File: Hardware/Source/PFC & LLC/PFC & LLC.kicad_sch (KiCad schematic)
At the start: 0 parts

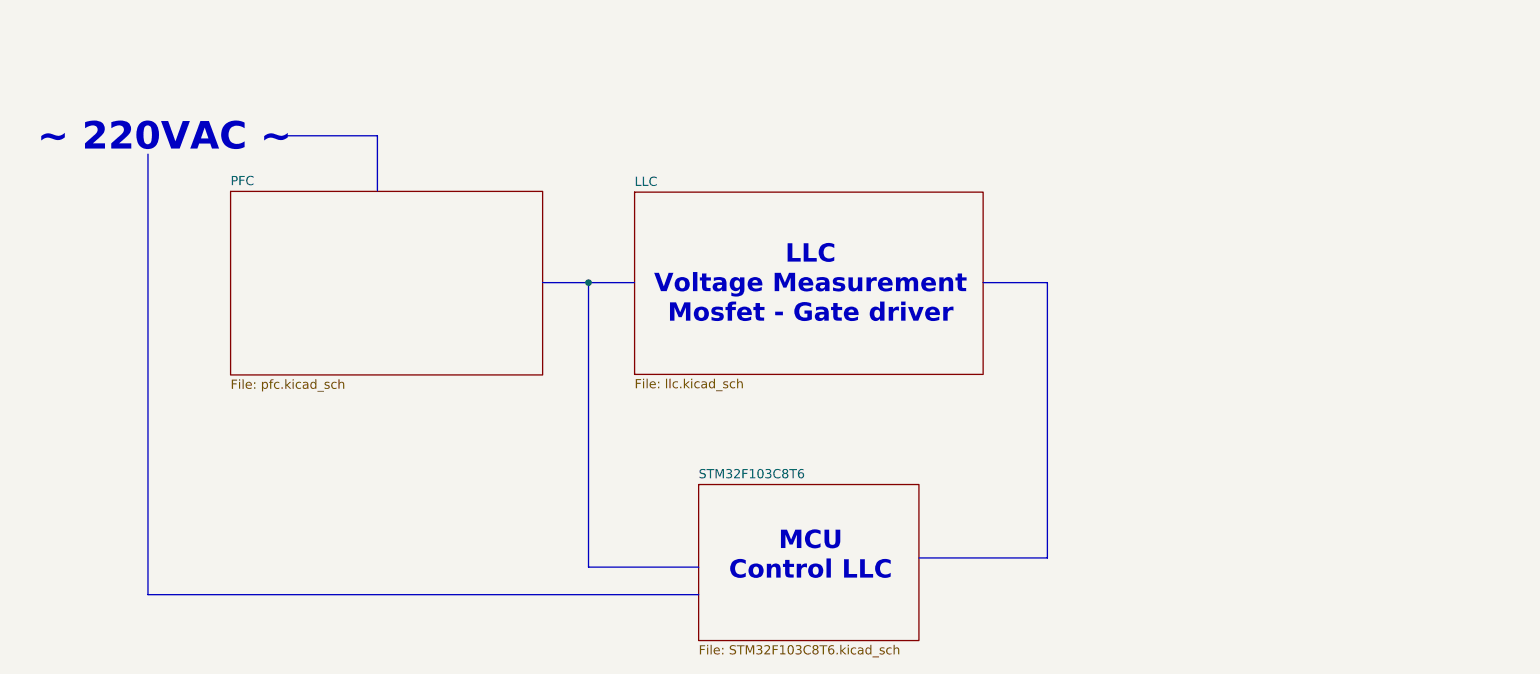
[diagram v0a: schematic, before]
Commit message: update ver 2.0 PFC-LLC
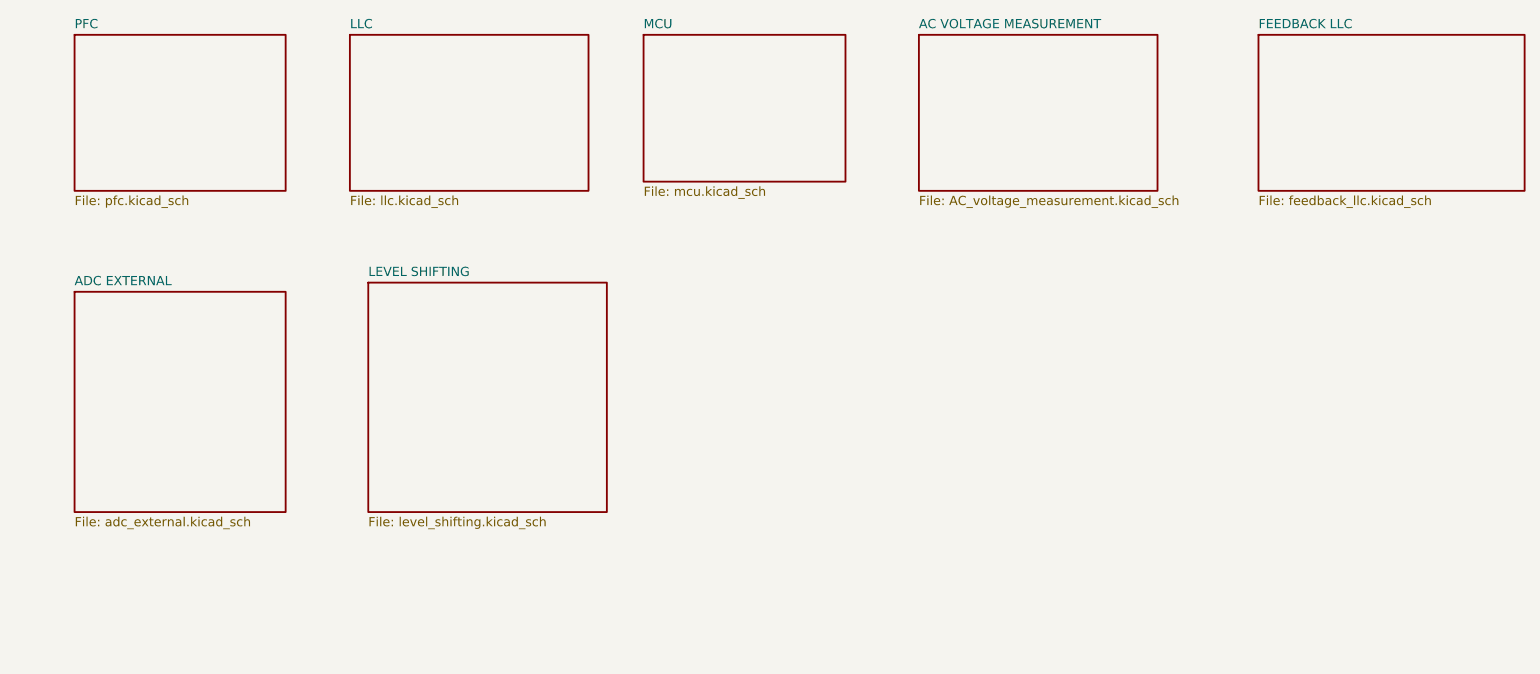
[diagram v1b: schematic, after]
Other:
- removed sheet STM32F103C8T6
- added sheet AC VOLTAGE MEASUREMENT (AC_voltage_measurement.kicad_sch)
- added sheet ADC EXTERNAL (adc_external.kicad_sch)
- added sheet FEEDBACK LLC (feedback_llc.kicad_sch)
- added sheet LEVEL SHIFTING (level_shifting.kicad_sch)
- added sheet MCU (mcu.kicad_sch)
- note removed: "LLC Voltage Measurement Mosfet - Gate driver"
- note removed: "MCU Control LLC"
- note removed: "~ 220VAC ~"
- company: (none) -> Ho Chi Minh City University of Technology - HCMUT
- title: (none) -> PFC & LLC

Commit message: update FEEDBACK, AC
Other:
- added sheet DETECT BATTERY (detect_battery.kicad_sch)
- added sheet POWER SUPPLY (power_supply.kicad_sch)
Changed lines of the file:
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@@
+	)
+	(sheet
+		(at 165.1 68.58)
+		(size 27.94 31.75)
+		(fields_autoplaced yes)
+		(stroke
+			(width 0.254)
+			(type solid)
+		)
+		(fill
+			(color 0 0 0 0.0000)
+		)
+		(property "Sheetname" "POWER SUPPLY"
+			(at 165.1 67.8176 0)
+			(effects
+				(font
+					(size 1.27 1.27)
+				)
+				(justify left bottom)
+			)
+		)
+		(property "Sheetfile" "power_supply.kicad_sch"
+			(at 165.1 100.9654 0)
+			(effects
+				(font
+					(size 1.27 1.27)
+				)
+				(justify left top)
+			)
+		)
+		(instances
+			(project "PFC & LLC"
+				(path "/97d1a1fe-d5a5-4da8-b78a-88a9132d14ad"
+					(page "10")
+				)
+			)
+		)
 	)
 	(sheet
@@
 				)
 			)
+		)
+	)
+	(sheet
+		(at 128.27 68.58)
+		(size 25.4 31.75)
+		(fields_autoplaced yes)
+		(stroke
+			(width 0.254)
+			(type solid)
+		)
+		(fill
+			(color 0 0 0 0.0000)
+		)
+		(property "Sheetname" "DETECT BATTERY"
+			(at 128.27 67.8176 0)
+			(effects
+				(font
+					(size 1.27 1.27)
+				)
+				(justify left bottom)
+			)
+		)
+		(property "Sheetfile" "detect_battery.kicad_sch"
+			(at 128.27 100.9654 0)
+			(effects
+				(font
+					(size 1.27 1.27)
+				)
+				(justify left top)
+			)
+		)
+		(instances
+			(project "PFC & LLC"
+				(path "/97d1a1fe-d5a5-4da8-b78a-88a9132d14ad"
+					(page "9")
+				)
+			)

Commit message: update lib, LLC
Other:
- added sheet ENABLE LLC PFC (enable_LLC_PFC.kicad_sch)
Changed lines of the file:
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@@
 	)
 	(sheet
-		(at 165.1 68.58)
-		(size 27.94 31.75)
+		(at 165.1 74.93)
+		(size 39.37 21.59)
 		(fields_autoplaced yes)
 		(stroke
@@
 		)
 		(property "Sheetname" "POWER SUPPLY"
-			(at 165.1 67.8176 0)
+			(at 165.1 74.1676 0)
 			(effects
 				(font
@@
 		)
 		(property "Sheetfile" "power_supply.kicad_sch"
-			(at 165.1 100.9654 0)
+			(at 165.1 97.1554 0)
 			(effects
 				(font
@@
 	)
 	(sheet
-		(at 212.09 34.29)
+		(at 210.82 34.29)
 		(size 36.83 21.59)
 		(fields_autoplaced yes)
@@
 		)
 		(property "Sheetname" "FEEDBACK LLC"
-			(at 212.09 33.5276 0)
+			(at 210.82 33.5276 0)
 			(effects
 				(font
@@
 		)
 		(property "Sheetfile" "feedback_llc.kicad_sch"
-			(at 212.09 56.5154 0)
+			(at 210.82 56.5154 0)
 			(effects
 				(font
@@
 	)
 	(sheet
-		(at 128.27 68.58)
-		(size 25.4 31.75)
+		(at 124.46 66.04)
+		(size 39.37 31.75)
 		(fields_autoplaced yes)
 		(stroke
@@
 		)
 		(property "Sheetname" "DETECT BATTERY"
-			(at 128.27 67.8176 0)
+			(at 124.46 65.2776 0)
 			(effects
 				(font
@@
 		)
 		(property "Sheetfile" "detect_battery.kicad_sch"
-			(at 128.27 100.9654 0)
+			(at 124.46 98.4254 0)
 			(effects
 				(font
@@
 	(sheet
 		(at 165.1 34.29)
-		(size 33.02 21.59)
+		(size 39.37 21.59)
 		(fields_autoplaced yes)
 		(stroke
@@
 				)
 			)
+		)
+	)
+	(sheet
+		(at 210.82 74.93)
+		(size 38.1 22.86)
+		(fields_autoplaced yes)
+		(stroke
+			(width 0.254)
+			(type solid)
+		)
+		(fill
+			(color 0 0 0 0.0000)
+		)
+		(property "Sheetname" "ENABLE LLC PFC"
+			(at 210.82 74.1676 0)
+			(effects
+				(font
+					(size 1.27 1.27)
+				)
+				(justify left bottom)
+			)
+		)
+		(property "Sheetfile" "enable_LLC_PFC.kicad_sch"
+			(at 210.82 98.4254 0)
+			(effects
+				(font
+					(size 1.27 1.27)
+				)
+				(justify left top)
+			)
+		)
+		(instances
+			(project "PFC & LLC"
+				(path "/97d1a1fe-d5a5-4da8-b78a-88a9132d14ad"
+					(page "11")
+				)
+			)
